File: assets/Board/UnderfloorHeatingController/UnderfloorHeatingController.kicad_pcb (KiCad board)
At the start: 2 copper layers, 173.7 x 52.3 mm, 56 parts, among them J10 Screw_Terminal_01x02, J11 Screw_Terminal_01x02, J12 Screw_Terminal_01x02, J13 Screw_Terminal_01x02, J14 Screw_Terminal_01x02, J15 Screw_Terminal_01x02, J16 Screw_Terminal_01x02, J2 Screw_Terminal_01x03, J3 Screw_Terminal_01x03, J5 Screw_Terminal_01x02, J6 Screw_Terminal_01x02, J7 Screw_Terminal_01x02, J8 Screw_Terminal_01x02, J9 Screw_Terminal_01x02, K1 G5Q-1A, Q1 BC337, U10 AQY214EH, U11 AQY214EH, U12 AQY214EH, U13 AQY214EH, U14 AQY214EH, U15 AQY214EH, U16 AQY214EH, U2 Waveshare_ESP32-S3-Tiny, U4 AQY214EH, U5 ACS725LLCTR-10AB-T, U6 AQY214EH, U7 AQY214EH, U8 AQY214EH, U9 AQY214EH

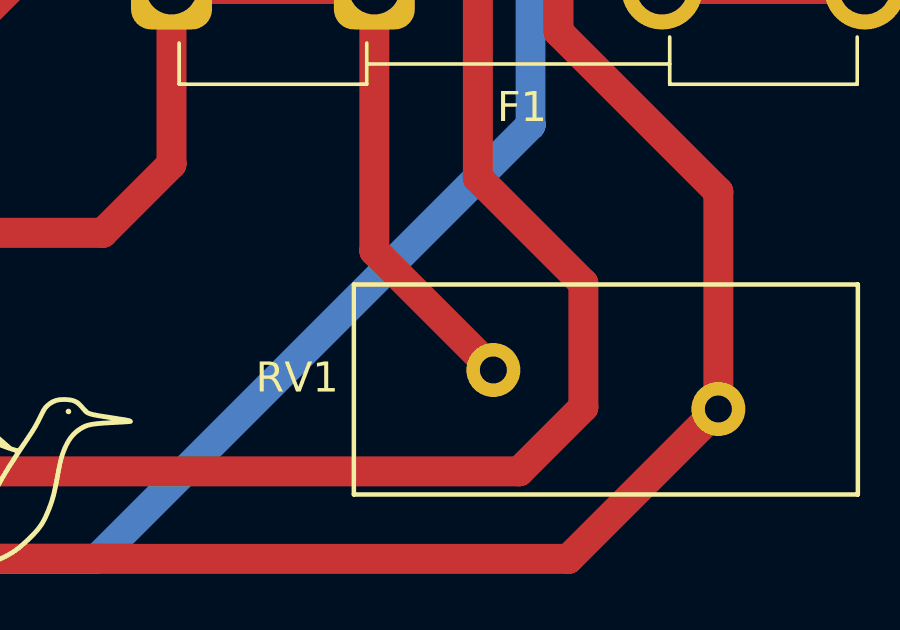
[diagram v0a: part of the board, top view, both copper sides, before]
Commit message: Migrated to the MDM server.
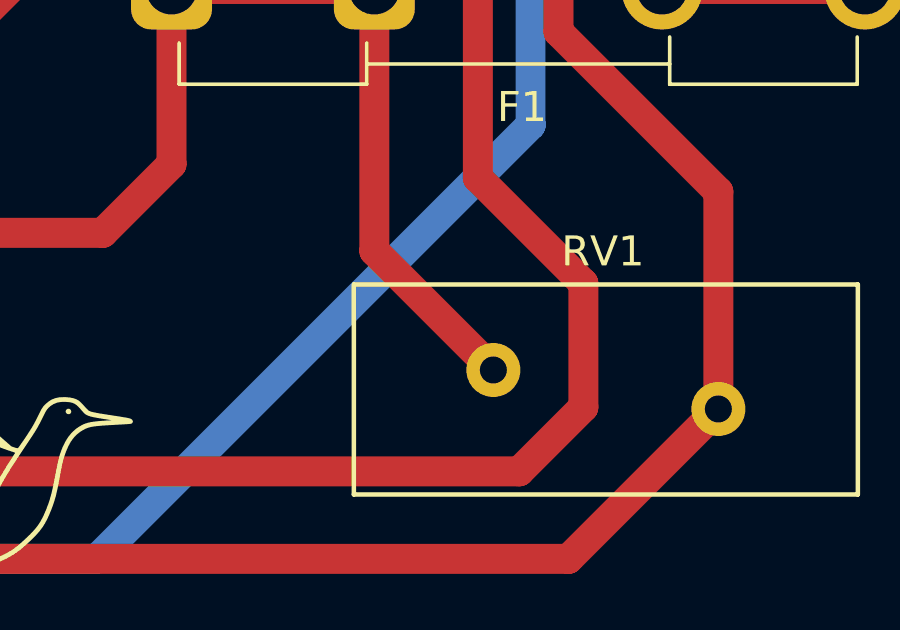
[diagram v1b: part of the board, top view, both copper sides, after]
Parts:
- C4: value 1nF -> 0.1µF
- R10, R11, R12, R13, R14, R15, R16, R5, R6, R7, R8, R9: value 2K -> 470
- RV1: footprint Custom Footprints:RV_Disc_D16.5mm_W6.7mm_P7.5mm with courtyard -> Varistor:RV_Disc_D16.5mm_W6.7mm_P7.5mm
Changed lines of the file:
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@@
 			)
 		)
-		(property "Value" "2K"
+		(property "Value" "470"
 			(at 0 1.65 0)
 			(layer "F.Fab")
@@
 		)
 	)
-	(footprint "Custom Footprints:RV_Disc_D16.5mm_W6.7mm_P7.5mm with courtyard"
+	(footprint "Varistor:RV_Disc_D16.5mm_W6.7mm_P7.5mm"
 		(layer "F.Cu")
 		(at 204.5335 108.204)
@@
 		(tags "varistor SIOV")
 		(property "Reference" "RV1"
-			(at -6.5405 0.254 0)
+			(at 3.65 -3.95 0)
 			(layer "F.SilkS")
 			(effects
@@
 			(layer "F.SilkS")
 		)
-		(fp_rect
-			(start -10.795 -9.017)
-			(end 18.288 10.287)
-			(stroke
-				(width 0.05)
-				(type solid)
-			)
-			(fill no)
-			(layer "B.CrtYd")
-		)
 		(fp_line
 			(start -4.75 -2.95)
@@
 			(layer "F.CrtYd")
 		)
-		(fp_rect
-			(start -10.795 -9.017)
-			(end 18.288 10.287)
-			(stroke
-				(width 0.05)
-				(type default)
-			)
-			(fill no)
-			(layer "F.CrtYd")
-		)
 		(fp_line
 			(start -4.5 -2.7)
@@
 			)
 		)
-		(property "Value" "2K"
+		(property "Value" "470"
 			(at 0 1.65 0)
 			(layer "F.Fab")
@@
 			)
 		)
-		(property "Value" "2K"
+		(property "Value" "470"
 			(at 0 1.65 0)
 			(layer "F.Fab")
@@
 			)
 		)
-		(property "Value" "2K"
+		(property "Value" "470"
 			(at 0 1.65 0)
 			(layer "F.Fab")
@@
 			)
 		)
-		(property "Value" "2K"
+		(property "Value" "470"
 			(at 0 1.65 0)
 			(layer "F.Fab")
@@
 			)
 		)
-		(property "Value" "2K"
+		(property "Value" "470"
 			(at 0 1.65 0)
 			(layer "F.Fab")
@@
 			)
 		)
-		(property "Value" "2K"
+		(property "Value" "470"
 			(at 0 1.65 0)
 			(layer "F.Fab")
@@
 			)
 		)
-		(property "Value" "2K"
+		(property "Value" "470"
 			(at 0 1.65 0)
 			(layer "F.Fab")
@@
 			)
 		)
-		(property "Value" "2K"
+		(property "Value" "470"
 			(at 0 1.65 0)
 			(layer "F.Fab")
@@
 			)
 		)
-		(property "Value" "2K"
+		(property "Value" "470"
 			(at 0 1.65 0)
 			(layer "F.Fab")
@@
 			)
 		)
-		(property "Value" "1nF"
+		(property "Value" "0.1µF"
 			(at 0 1.68 90)
 			(layer "F.Fab")
@@
 			)
 		)
-		(property "Value" "2K"
+		(property "Value" "470"
 			(at 0 1.65 0)
 			(layer "F.Fab")
@@
 			)
 		)
-		(property "Value" "2K"
+		(property "Value" "470"
 			(at 0 1.65 0)
 			(layer "F.Fab")

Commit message: First version of the redesigned controller.
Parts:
- removed D1: 1N4007, Diode_THT:D_DO-35_SOD27_P7.62mm_Horizontal
- removed J15, J16: Screw_Terminal_01x02, TerminalBlock_Phoenix:TerminalBlock_Phoenix_MKDS-1,5-2-5.08_1x02_P5.08mm_Horizontal
- removed Q1: BC337, Package_TO_SOT_THT:TO-92_Inline
- removed U10, U11, U12, U13, U14, U15, U16, U7, U8, U9: AQY214EH, Package_DIP:DIP-4_W7.62mm
- added C10: 10u, Capacitor_SMD:C_0805_2012Metric_Pad1.18x1.45mm_HandSolder, F.Cu at (72.0, 103.6)
- added C11: 0.01u, Capacitor_SMD:C_0805_2012Metric_Pad1.18x1.45mm_HandSolder, F.Cu at (90.5, 59.2)
- added C12: 2.2u, Capacitor_SMD:C_0805_2012Metric_Pad1.18x1.45mm_HandSolder, F.Cu at (90.5, 62.2)
- added C13: 10u, Capacitor_SMD:C_0805_2012Metric_Pad1.18x1.45mm_HandSolder, F.Cu at (90.5, 65.2)
- added C14: 0.01u, Capacitor_SMD:C_0805_2012Metric_Pad1.18x1.45mm_HandSolder, F.Cu at (39.6, 97.6)
- added C15: 2.2u, Capacitor_SMD:C_0805_2012Metric_Pad1.18x1.45mm_HandSolder, F.Cu at (39.6, 100.6)
- added C16: 2.2u, Capacitor_SMD:C_0805_2012Metric_Pad1.18x1.45mm_HandSolder, F.Cu at (104.4, 94.0)
- added C17: 10u, Capacitor_SMD:C_0805_2012Metric_Pad1.18x1.45mm_HandSolder, F.Cu at (104.4, 97.0)
- added C18: 10u, Capacitor_SMD:C_0805_2012Metric_Pad1.18x1.45mm_HandSolder, F.Cu at (39.6, 103.6)
- added C6: 68n, Capacitor_SMD:C_0805_2012Metric_Pad1.18x1.45mm_HandSolder, F.Cu at (93.8, 122.9)
- added C7: 0.01u, Capacitor_SMD:C_0805_2012Metric_Pad1.18x1.45mm_HandSolder, F.Cu at (104.4, 91.0)
- added C8: 0.01u, Capacitor_SMD:C_0805_2012Metric_Pad1.18x1.45mm_HandSolder, F.Cu at (72.0, 97.6)
- added C9: 2.2u, Capacitor_SMD:C_0805_2012Metric_Pad1.18x1.45mm_HandSolder, F.Cu at (72.0, 100.6)
- added J1: Screw_Terminal_01x02, TerminalBlock_Phoenix:TerminalBlock_Phoenix_MKDS-1,5-2-5.08_1x02_P5.08mm_Horizontal, F.Cu at (19.5, 57.3)
- added J4: Screw_Terminal_01x02, TerminalBlock_Phoenix:TerminalBlock_Phoenix_MKDS-1,5-2-5.08_1x02_P5.08mm_Horizontal, F.Cu at (19.5, 69.5)
- added K2: Relay_SPST_Latching_1coil, Custom Footprints:Relay_SPST_Hongfa_HF3F-L-xx-1HL1T (custom), F.Cu at (53.1, 92.0)
- added K3: Relay_SPST_Latching_1coil, Custom Footprints:Relay_SPST_Hongfa_HF3F-L-xx-1HL1T (custom), F.Cu at (53.1, 109.3)
- added K4: Relay_SPST_Latching_1coil, Custom Footprints:Relay_SPST_Hongfa_HF3F-L-xx-1HL1T (custom), F.Cu at (71.6, 53.6)
- added K5: Relay_SPST_Latching_1coil, Custom Footprints:Relay_SPST_Hongfa_HF3F-L-xx-1HL1T (custom), F.Cu at (71.6, 70.9)
- added K6: Relay_SPST_Latching_1coil, Custom Footprints:Relay_SPST_Hongfa_HF3F-L-xx-1HL1T (custom), F.Cu at (20.7, 92.0)
- added K7: Relay_SPST_Latching_1coil, Custom Footprints:Relay_SPST_Hongfa_HF3F-L-xx-1HL1T (custom), F.Cu at (20.7, 109.3)
- added U1: BL0937B, Package_SO:JEITA_SOIC-8_3.9x4.9mm_P1.27mm, F.Cu at (95.6, 127.7)
- added U3: DRV8833PWR, Package_SO:TSSOP-16_4.4x5mm_P0.65mm, F.Cu at (74.4, 92.8)
- C2, C4: value 0.1µF -> 68n
- K1: value G5Q-1A -> Relay_SPST_Latching_1coil; footprint Relay_THT:Relay_SPST_Omron-G5Q-1A -> Custom Footprints:Relay_SPST_Hongfa_HF3F-L-xx-1HL1T (custom)
- R10: value 470 -> 510
- R11: value 470 -> 1m; footprint Resistor_SMD:R_0805_2012Metric_Pad1.20x1.40mm_HandSolder -> Resistor_SMD:R_Shunt_Vishay_WSKW0612
- R12, R13, R14, R15: value 470 -> 47k
- R16: value 470 -> 0
- R2: value 560 -> 510
- R3: value 100K -> 510
- R4: value 100 -> 200K; footprint Resistor_SMD:R_0805_2012Metric_Pad1.20x1.40mm_HandSolder -> Resistor_SMD:R_1206_3216Metric_Pad1.30x1.75mm_HandSolder
- R5, R6, R7, R8, R9: value 470 -> 200K; footprint Resistor_SMD:R_0805_2012Metric_Pad1.20x1.40mm_HandSolder -> Resistor_SMD:R_1206_3216Metric_Pad1.30x1.75mm_HandSolder
- U4, U6: value AQY214EH -> DRV8833PWR; footprint Package_DIP:DIP-4_W7.62mm -> Package_SO:TSSOP-16_4.4x5mm_P0.65mm
- U5: value ACS725LLCTR-10AB-T -> DRV8833PWR; footprint Package_SO:SOIC-8_3.9x4.9mm_P1.27mm -> Package_SO:TSSOP-16_4.4x5mm_P0.65mm
- moved U5 100.2 mm to (92.8, 54.4), turned to 0 degrees
- moved R4 90.8 mm to (83.7, 117.0)
- moved C4 84.0 mm to (93.8, 119.9), turned to 0 degrees
- moved C2 83.1 mm to (93.8, 116.8), turned to 0 degrees
- moved R3 82.9 mm to (89.0, 119.8), turned to 0 degrees
- moved R2 80.5 mm to (89.0, 116.8), turned to 0 degrees
- moved J10 71.9 mm to (43.9, 69.5), turned to 0 degrees
- moved K1 68.6 mm to (85.5, 92.0), turned to 0 degrees
- moved R15 65.6 mm to (39.6, 106.6)
- moved F1 63.5 mm to (247.7, 129.2)
- moved RV1 63.1 mm to (251.5, 150.5)
- moved J9 62.3 mm to (43.9, 57.3), turned to 0 degrees
- moved J8 61.8 mm to (31.7, 81.6), turned to 0 degrees
- moved J2 59.0 mm to (266.1, 107.3)
- moved J12 54.5 mm to (56.1, 57.3)
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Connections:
- C2 pad 1: +3V3 -> Net-(U1-IN)
- C4 pad 1: Net-(U5-FILTER) -> GND
- C4 pad 2: GND -> Net-(U1-IP)
- J10 pad 1: /ETA_MATRIX/ETA6/POWER_L_ETA -> /ETA relays/Relay pair - ETA2/POWER_RELAY_B
- J10 pad 2: POWER_N -> POWER_N_MON
- J11 pad 1: /ETA_MATRIX/ETA7/POWER_L_ETA -> /ETA relays/Relay pair - ETA3/POWER_RELAY_A
- J11 pad 2: POWER_N -> POWER_N_MON
- J12 pad 1: /ETA_MATRIX/ETA8/POWER_L_ETA -> /ETA relays/Relay pair - ETA3/POWER_RELAY_A
- J12 pad 2: POWER_N -> POWER_N_MON
- J13 pad 1: /ETA_MATRIX/ETA9/POWER_L_ETA -> /ETA relays/Relay pair - ETA3/POWER_RELAY_A
- J13 pad 2: POWER_N -> POWER_N_MON
- J14 pad 1: /ETA_MATRIX/ETA10/POWER_L_ETA -> /ETA relays/Relay pair - ETA3/POWER_RELAY_B
- J14 pad 2: POWER_N -> POWER_N_MON
- J3 pad 2: POWER_N -> POWER_N_MON
- J5 pad 1: /ETA_MATRIX/ETA1/POWER_L_ETA -> /ETA relays/Relay pair - ETA1/POWER_RELAY_B
- J5 pad 2: POWER_N -> POWER_N_MON
- J6 pad 1: /ETA_MATRIX/ETA2/POWER_L_ETA -> /ETA relays/Relay pair - ETA1/POWER_RELAY_B
- J6 pad 2: POWER_N -> POWER_N_MON
- J7 pad 1: /ETA_MATRIX/ETA3/POWER_L_ETA -> /ETA relays/Relay pair - ETA2/POWER_RELAY_A
- J7 pad 2: POWER_N -> POWER_N_MON
- J8 pad 1: /ETA_MATRIX/ETA4/POWER_L_ETA -> /ETA relays/Relay pair - ETA2/POWER_RELAY_A
- J8 pad 2: POWER_N -> POWER_N_MON
- J9 pad 1: /ETA_MATRIX/ETA5/POWER_L_ETA -> /ETA relays/Relay pair - ETA2/POWER_RELAY_B
- J9 pad 2: POWER_N -> POWER_N_MON
- PS1 pad 1: POWER_L_MON -> POWER_L
- PS1 pad 2: POWER_N -> POWER_N_MON
- R1 pad 1: POWER_L_MON -> POWER_L
- R10 pad 1: Net-(R10-Pad1) -> Net-(U1-VP)
- R10 pad 2: ETA_L6 -> GND
- R11 pad 1: Net-(R11-Pad1) -> POWER_N
- R11 pad 2: ETA_L7 -> POWER_N
- R12 pad 1: Net-(R12-Pad1) -> +5V
- R12 pad 2: ETA_L8 -> Net-(U4-~{SLEEP})
- R13 pad 1: Net-(R13-Pad1) -> +5V
- R13 pad 2: ETA_L9 -> Net-(U3-~{SLEEP})
- R14 pad 1: Net-(R14-Pad1) -> +5V
- R14 pad 2: ETA_L10 -> Net-(U5-~{SLEEP})
- R15 pad 1: Net-(R15-Pad1) -> +5V
- R15 pad 2: ETA_L11 -> Net-(U6-~{SLEEP})
- R16 pad 1: Net-(R16-Pad1) -> POWER_N
- R16 pad 2: ETA_L12 -> GND
- R2 pad 1: Net-(Q1-B) -> POWER_N
- R2 pad 2: MOTOR_CTRL -> Net-(U1-IN)
- R3 pad 1: GND -> POWER_N_MON
- R3 pad 2: Net-(Q1-B) -> Net-(U1-IP)
- R4 pad 1: CURRENT_MON -> POWER_L
- R4 pad 2: Net-(U5-VIOUT) -> Net-(R4-Pad2)
- R5 pad 1: Net-(R5-Pad1) -> Net-(R4-Pad2)
- R5 pad 2: ETA_L1 -> Net-(R5-Pad2)
- R6 pad 1: Net-(R6-Pad1) -> Net-(R5-Pad2)
- R6 pad 2: ETA_L2 -> Net-(R6-Pad2)
- R7 pad 1: Net-(R7-Pad1) -> Net-(R6-Pad2)
- R7 pad 2: ETA_L3 -> Net-(R7-Pad2)
- R8 pad 1: Net-(R8-Pad1) -> Net-(R7-Pad2)
- R8 pad 2: ETA_L4 -> Net-(R8-Pad2)
- R9 pad 1: Net-(R9-Pad1) -> Net-(R8-Pad2)
- R9 pad 2: ETA_L5 -> Net-(U1-VP)
- U2 pad 10: ETA_L2 -> RELAY_ETA1_A_IN1
- U2 pad 11: ETA_L1 -> RELAY_ETA1_A_IN2
- U2 pad 12: ETA_L7 -> RELAY_ETA1_B_IN1
- U2 pad 13: ETA_L8 -> RELAY_ETA1_B_IN2
- U2 pad 14: ETA_L9 -> RELAY_ETA2_A_IN1
- U2 pad 15: ETA_L10 -> RELAY_ETA2_A_IN2
- U2 pad 16: ETA_L11 -> RELAY_ETA2_B_IN1
- U2 pad 17: ETA_L12 -> RELAY_ETA2_B_IN2
- U2 pad 18: unconnected-(U2-15-Pad18) -> RELAY_ETA3_A_IN1
- U2 pad 19: unconnected-(U2-16-Pad19) -> RELAY_ETA3_A_IN2
- U2 pad 20: unconnected-(U2-17-Pad20) -> RELAY_ETA3_B_IN1
- U2 pad 21: unconnected-(U2-18-Pad21) -> RELAY_ETA3_B_IN2
- U2 pad 4: CURRENT_MON -> MON_CF
- U2 pad 5: MOTOR_CTRL -> MON_CF1
- U2 pad 6: ETA_L6 -> MON_SEL
- U2 pad 7: ETA_L5 -> RELAY_FAULT
- U2 pad 8: ETA_L4 -> RELAY_MOTOR_IN1
- U2 pad 9: ETA_L3 -> RELAY_MOTOR_IN2
- U4 pad 1: Net-(R5-Pad1) -> Net-(U4-~{SLEEP})
- U4 pad 2: GND -> Net-(U4-AOUT1)
- U4 pad 3: /ETA_MATRIX/ETA1/POWER_L_ETA -> GND
- U4 pad 4: POWER_L_MON -> Net-(U4-AOUT2)
- U5 pad 1: POWER_L -> Net-(U5-~{SLEEP})
- U5 pad 2: POWER_L -> Net-(U5-AOUT1)
- U5 pad 3: POWER_L_MON -> GND
- U5 pad 4: POWER_L_MON -> Net-(U5-AOUT2)
- U5 pad 5: GND -> Net-(U5-BOUT2)
- U5 pad 6: Net-(U5-FILTER) -> GND
- U5 pad 7: Net-(U5-VIOUT) -> Net-(U5-BOUT1)
- U5 pad 8: +3V3 -> RELAY_FAULT
- U6 pad 1: Net-(R6-Pad1) -> Net-(U6-~{SLEEP})
- U6 pad 2: GND -> Net-(U6-AOUT1)
- U6 pad 3: /ETA_MATRIX/ETA2/POWER_L_ETA -> GND
- U6 pad 4: POWER_L_MON -> Net-(U6-AOUT2)
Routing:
- net POWER_N: track 363.6 -> 0.00 mm
- net POWER_L_MON: track 325.9 -> 0.00 mm, vias 5 -> 0
- net POWER_PE: track 113.8 -> 0.00 mm
- net ETA_L1: track 89.7 -> 0.00 mm
- net ETA_L7: track 80.0 -> 0.00 mm
- net ETA_L2: track 78.5 -> 0.00 mm
- net ETA_L3: track 68.5 -> 0.00 mm
- net +3V3: track 68.1 -> 0.00 mm, vias 2 -> 0
- net MOTOR_CTRL: track 67.1 -> 0.00 mm, vias 2 -> 0
- net ETA_L8: track 66.4 -> 0.00 mm
- net CURRENT_MON: track 64.9 -> 0.00 mm, vias 2 -> 0
- net ETA_L4: track 63.0 -> 0.00 mm
- net ETA_L5: track 54.0 -> 0.00 mm
- net +5V: track 51.2 -> 0.00 mm
- net ETA_L9: track 51.1 -> 0.00 mm
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- removed copper zone on B.Cu, net GND
- removed copper zone on F.Cu, net GND
- removed copper zone on B.Cu, net POWER_L
- removed copper zone on F.Cu, net POWER_L
- removed copper zone on B.Cu, net POWER_L_MON
- removed copper zone on F.Cu, net POWER_L_MON
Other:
- board text added: "UNDERFLOOR HEATING CONTROLLER 2026-02-22 ¦ v2 | HV 200W rating"
- board text removed: "UNDERFLOOR HEATING CONTROLLER 2025-12-06 ¦ v1 | HV 200W rating"

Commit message: Fully routed board.
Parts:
- removed R12, R13, R14, R15: 47k, Resistor_SMD:R_0805_2012Metric_Pad1.20x1.40mm_HandSolder
- added C19: 0.1uF, Capacitor_SMD:C_0805_2012Metric_Pad1.18x1.45mm_HandSolder, F.Cu at (159.0, 53.1)
- added C20: 10uF, Capacitor_SMD:C_0805_2012Metric_Pad1.18x1.45mm_HandSolder, F.Cu at (159.5, 49.5)
- C1: value 1000µF -> 1000uF
- C10, C13, C17, C18: value 10u -> 10uF
- C11, C14, C7, C8: value 0.01u -> 0.01uF
- C12, C15, C16, C9: value 2.2u -> 2.2uF
- C2, C4, C6: value 68n -> 68nF
- C3: value 0.1µF -> 0.1uF
- moved R9 125.7 mm to (174.2, 46.4), turned to 180 degrees
- moved R8 121.7 mm to (174.2, 49.0)
- moved R7 117.8 mm to (174.2, 51.6), turned to 180 degrees
- moved R10 116.0 mm to (174.2, 43.9)
- moved C6 114.3 mm to (174.2, 41.7)
- moved R6 114.1 mm to (174.2, 54.2)
- moved R5 110.6 mm to (174.2, 56.8), turned to 180 degrees
- moved RV1 108.6 mm to (174.1, 74.2), turned to -90 degrees
- moved R4 107.3 mm to (174.2, 59.4)
- moved PS1 104.7 mm to (139.7, 99.6), turned to 90 degrees
- moved U1 103.2 mm to (164.1, 50.5), turned to 90 degrees
- moved R16 101.8 mm to (168.7, 62.2), turned to 90 degrees
- moved F1 101.4 mm to (160.0, 78.1), turned to -90 degrees
- moved R11 101.3 mm to (164.0, 64.2), turned to 90 degrees
- moved J2 95.5 mm to (170.7, 103.4)
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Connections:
- C2 pad 1: Net-(U1-IN) -> Net-(U1-IP)
- C4 pad 2: Net-(U1-IP) -> Net-(U1-IN)
- J2 pad 1: POWER_L_UNFUSED -> POWER_PE
- J2 pad 2: POWER_N -> POWER_L_UNFUSED
- J2 pad 3: POWER_PE -> POWER_N
- J3 pad 1: POWER_PE -> POWER_L_MOTOR
- J3 pad 3: POWER_L_MOTOR -> POWER_PE
- K1 pad A1: Net-(U4-AOUT1) -> Net-(U4-AOUT2)
- K1 pad A2: Net-(U4-AOUT2) -> Net-(U4-AOUT1)
- K2 pad A1: Net-(U3-AOUT1) -> Net-(U3-AOUT2)
- K2 pad A2: Net-(U3-AOUT2) -> Net-(U3-AOUT1)
- K4 pad A1: Net-(U5-AOUT1) -> Net-(U5-AOUT2)
- K4 pad A2: Net-(U5-AOUT2) -> Net-(U5-AOUT1)
- K6 pad A1: Net-(U6-AOUT1) -> Net-(U6-AOUT2)
- K6 pad A2: Net-(U6-AOUT2) -> Net-(U6-AOUT1)
- PS1 pad 2: POWER_N_MON -> POWER_N
- R11 pad 1: POWER_N -> POWER_N_MON
- R11 pad 2: POWER_N -> MON_CURRENT_SENSE_2
- R11 pad 3: POWER_N_MON -> MON_CURRENT_SENSE_1
- R11 pad 4: POWER_N_MON -> POWER_N
- R2 pad 1: POWER_N -> MON_CURRENT_SENSE_1
- R2 pad 2: Net-(U1-IN) -> Net-(U1-IP)
- R3 pad 1: POWER_N_MON -> MON_CURRENT_SENSE_2
- R3 pad 2: Net-(U1-IP) -> Net-(U1-IN)
- U2 pad 10: RELAY_ETA1_A_IN1 -> RELAY_MOTOR_IN2
- U2 pad 11: RELAY_ETA1_A_IN2 -> RELAY_MOTOR_IN1
- U2 pad 12: RELAY_ETA1_B_IN1 -> RELAY_ETA3_A_IN2
- U2 pad 13: RELAY_ETA1_B_IN2 -> RELAY_ETA3_A_IN1
- U2 pad 14: RELAY_ETA2_A_IN1 -> RELAY_FAULT
- U2 pad 15: RELAY_ETA2_A_IN2 -> RELAY_ETA1_A_IN1
- U2 pad 16: RELAY_ETA2_B_IN1 -> RELAY_ETA1_A_IN2
- U2 pad 17: RELAY_ETA2_B_IN2 -> RELAY_ETA2_A_IN1
- U2 pad 18: RELAY_ETA3_A_IN1 -> RELAY_ETA2_A_IN2
- U2 pad 19: RELAY_ETA3_A_IN2 -> MON_SEL
- U2 pad 20: RELAY_ETA3_B_IN1 -> MON_CF1
- U2 pad 21: RELAY_ETA3_B_IN2 -> MON_CF
- U2 pad 4: MON_CF -> RELAY_ETA1_B_IN2
- U2 pad 5: MON_CF1 -> RELAY_ETA1_B_IN1
- U2 pad 6: MON_SEL -> RELAY_ETA2_B_IN2
- U2 pad 7: RELAY_FAULT -> RELAY_ETA2_B_IN1
- U2 pad 8: RELAY_MOTOR_IN1 -> RELAY_ETA3_B_IN2
- U2 pad 9: RELAY_MOTOR_IN2 -> RELAY_ETA3_B_IN1
- U3 pad 1: Net-(U3-~{SLEEP}) -> +5V
- U4 pad 1: Net-(U4-~{SLEEP}) -> +5V
- U5 pad 1: Net-(U5-~{SLEEP}) -> +5V
- U6 pad 1: Net-(U6-~{SLEEP}) -> +5V
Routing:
- net POWER_N_MON: track 0.00 -> 319.7 mm
- net POWER_L: track 0.00 -> 292.5 mm
- net +5V: track 0.00 -> 153.7 mm, vias 0 -> 8
- net Net-(U5-BOUT2): track 0.00 -> 75.8 mm, vias 0 -> 1
- net Net-(U5-AOUT2): track 0.00 -> 74.5 mm, vias 0 -> 1
- net POWER_N: track 0.00 -> 65.5 mm
- net Net-(U5-BOUT1): track 0.00 -> 64.5 mm, vias 0 -> 1
- net Net-(U6-AOUT1): track 0.00 -> 63.1 mm
- net Net-(U5-AOUT1): track 0.00 -> 59.8 mm, vias 0 -> 1
- net RELAY_ETA1_A_IN1: track 0.00 -> 54.2 mm, vias 0 -> 2
- net RELAY_ETA1_A_IN2: track 0.00 -> 52.6 mm, vias 0 -> 2
- net Net-(U6-AOUT2): track 0.00 -> 52.0 mm
- net Net-(U3-BOUT1): track 0.00 -> 51.6 mm, vias 0 -> 1
- net POWER_PE: track 0.00 -> 48.8 mm
- net RELAY_FAULT: track 0.00 -> 48.7 mm, vias 0 -> 5
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- added copper zone on B.Cu, net GND
- added copper zone on F.Cu, net GND
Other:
- board size 173.7 x 52.3 mm -> 141.5 x 70.4 mm
- board text added: "UNDERFLOOR HEATING CONTROLLER 2026-02-22 ¦ v2 | HV 700W rating"
- board text removed: "UNDERFLOOR HEATING CONTROLLER 2026-02-22 ¦ v2 | HV 200W rating"

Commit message: More tweaking.
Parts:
- moved R4 7.48 mm to (174.2, 66.9)
- moved R5 5.61 mm to (174.2, 62.4)
- moved R6 3.74 mm to (174.2, 58.0)
- moved R7 1.87 mm to (174.2, 53.5)
- moved R16 1.64 mm to (167.6, 61.0)
- moved RV1 1.33 mm to (174.1, 75.6)
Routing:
- net POWER_L: track 292.5 -> 285.8 mm
- net GND: track 8.59 -> 3.74 mm, vias 86 -> 93
- net POWER_N: track 65.5 -> 68.0 mm
- net Net-(R5-Pad2): track 2.43 -> 4.49 mm
- net Net-(R7-Pad2): track 2.61 -> 4.49 mm
- net Net-(R6-Pad2): track 2.61 -> 4.49 mm
- net Net-(R4-Pad2): track 2.61 -> 4.49 mm
- net Net-(U1-IP): track 12.0 -> 10.4 mm, vias 0 -> 2
